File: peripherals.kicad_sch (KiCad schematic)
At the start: 6 parts, among them Q1 BSS138, SW2 SW_ACK, U7 TSOP384xx

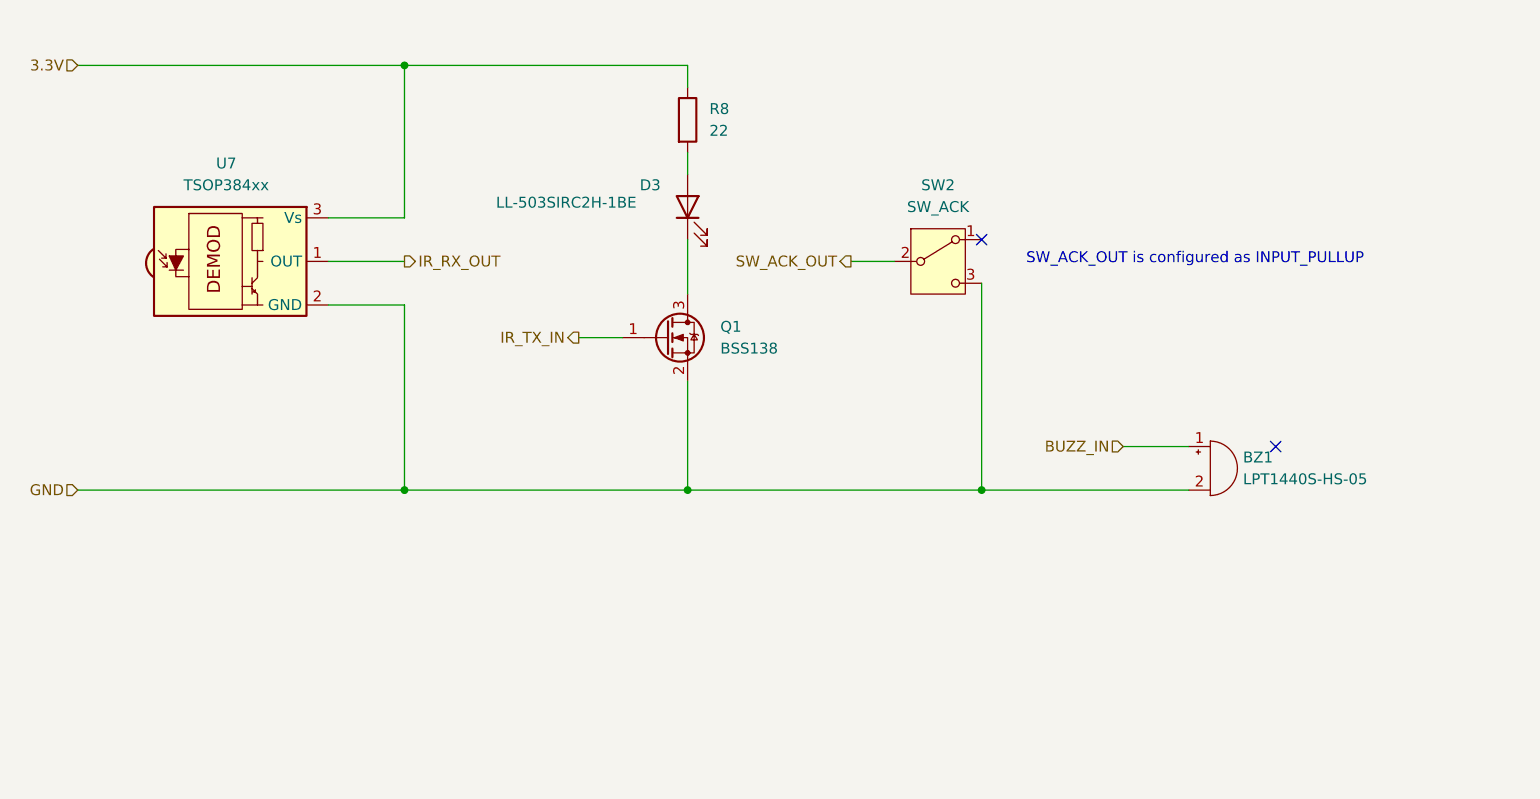
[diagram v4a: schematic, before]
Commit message: Cap and resistor for TSOP384x
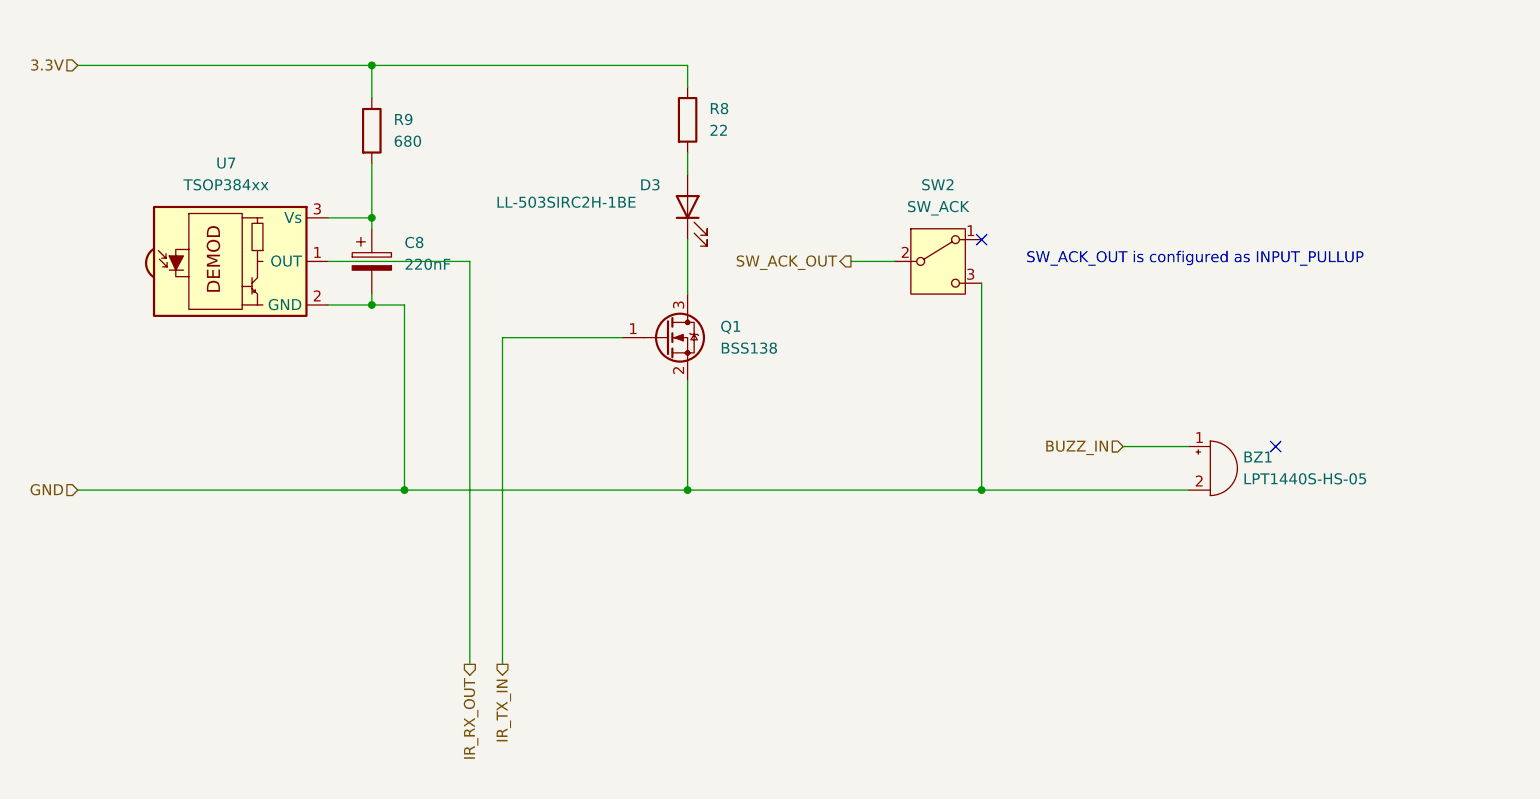
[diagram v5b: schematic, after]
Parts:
- added C8: 220nF, symbol Device:C_Polarized
- added R9: 680, symbol Device:R
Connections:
- net 3.3V: now also R9.1; no longer U7.3 (Vs)
- net GND: now also C8.2
- new net: C8.1, R9.2, U7.3 (Vs)
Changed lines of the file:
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@@
 	)
 	(junction
-		(at 81.28 38.1)
+		(at 77.47 38.1)
 		(diameter 0)
 		(color 0 0 0 0)
@@
 	)
 	(junction
+		(at 77.47 66.04)
+		(diameter 0)
+		(color 0 0 0 0)
+	)
+	(junction
 		(at 148.59 87.63)
 		(diameter 0)
@@
 		(color 0 0 0 0)
 	)
+	(junction
+		(at 77.47 55.88)
+		(diameter 0)
+		(color 0 0 0 0)
+	)
 	(no_connect
 		(at 148.59 58.42)
@@
 	(wire
 		(pts
-			(xy 101.6 69.85) (xy 106.68 69.85)
+			(xy 77.47 55.88) (xy 77.47 49.53)
 		)
 		(stroke
@@
 	(wire
 		(pts
+			(xy 77.47 64.77) (xy 77.47 66.04)
+		)
+		(stroke
+			(width 0)
+			(type default)
+		)
+	)
+	(wire
+		(pts
+			(xy 77.47 55.88) (xy 77.47 57.15)
+		)
+		(stroke
+			(width 0)
+			(type default)
+		)
+	)
+	(wire
+		(pts
 			(xy 114.3 74.93) (xy 114.3 87.63)
 		)
@@
 	(wire
 		(pts
+			(xy 92.71 69.85) (xy 92.71 107.95)
+		)
+		(stroke
+			(width 0)
+			(type default)
+		)
+	)
+	(wire
+		(pts
+			(xy 72.39 55.88) (xy 77.47 55.88)
+		)
+		(stroke
+			(width 0)
+			(type default)
+		)
+	)
+	(wire
+		(pts
+			(xy 77.47 66.04) (xy 81.28 66.04)
+		)
+		(stroke
+			(width 0)
+			(type default)
+		)
+	)
+	(wire
+		(pts
+			(xy 77.47 38.1) (xy 114.3 38.1)
+		)
+		(stroke
+			(width 0)
+			(type default)
+		)
+	)
+	(wire
+		(pts
+			(xy 88.9 60.96) (xy 88.9 107.95)
+		)
+		(stroke
+			(width 0)
+			(type default)
+		)
+	)
+	(wire
+		(pts
 			(xy 165.1 82.55) (xy 172.72 82.55)
 		)
@@
 	(wire
 		(pts
-			(xy 72.39 60.96) (xy 81.28 60.96)
-		)
-		(stroke
-			(width 0)
-			(type default)
-		)
-	)
-	(wire
-		(pts
-			(xy 81.28 38.1) (xy 114.3 38.1)
-		)
-		(stroke
-			(width 0)
-			(type default)
-		)
-	)
-	(wire
-		(pts
-			(xy 81.28 55.88) (xy 81.28 38.1)
+			(xy 92.71 69.85) (xy 106.68 69.85)
+		)
+		(stroke
+			(width 0)
+			(type default)
+		)
+	)
+	(wire
+		(pts
+			(xy 72.39 60.96) (xy 88.9 60.96)
+		)
+		(stroke
+			(width 0)
+			(type default)
+		)
+	)
+	(wire
+		(pts
+			(xy 43.18 38.1) (xy 77.47 38.1)
 		)
 		(stroke
@@
 	(wire
 		(pts
-			(xy 81.28 38.1) (xy 43.18 38.1)
+			(xy 77.47 38.1) (xy 77.47 41.91)
 		)
 		(stroke
@@
 	(wire
 		(pts
-			(xy 72.39 66.04) (xy 81.28 66.04)
-		)
-		(stroke
-			(width 0)
-			(type default)
-		)
-	)
-	(wire
-		(pts
-			(xy 72.39 55.88) (xy 81.28 55.88)
+			(xy 72.39 66.04) (xy 77.47 66.04)
 		)
 		(stroke
@@
 	(hierarchical_label "IR_RX_OUT"
 		(shape output)
-		(at 81.28 60.96 0)
+		(at 88.9 107.95 270)
 		(effects
 			(font
 				(size 1.27 1.27)
 			)
-			(justify left)
+			(justify right)
 		)
 	)
 	(hierarchical_label "IR_TX_IN"
 		(shape output)
-		(at 101.6 69.85 180)
+		(at 92.71 107.95 270)
 		(effects
 			(font
@@
 	)
 	(symbol
+		(lib_id "Device:R")
+		(at 77.47 45.72 0)
+		(unit 1)
+		(exclude_from_sim no)
+		(in_bom yes)
+		(on_board yes)
+		(dnp no)
+		(fields_autoplaced yes)
+		(property "Reference" "R9"
+			(at 80.01 44.4499 0)
+			(effects
+				(font
+					(size 1.27 1.27)
+				)
+				(justify left)
+			)
+		)
+		(property "Value" "680"
+			(at 80.01 46.9899 0)
+			(effects
+				(font
+					(size 1.27 1.27)
+				)
+				(justify left)
+			)
+		)
+		(property "Footprint" ""
+			(at 75.692 45.72 90)
+			(effects
+				(font
+					(size 1.27 1.27)
+				)
+				(hide yes)
+			)
+		)
+		(property "Datasheet" "~"
+			(at 77.47 45.72 0)
+			(effects
+				(font
+					(size 1.27 1.27)
+				)
+				(hide yes)
+			)
+		)
+		(property "Description" "Resistor"
+			(at 77.47 45.72 0)
+			(effects
+				(font
+					(size 1.27 1.27)
+				)
+				(hide yes)
+			)
+		)
+		(pin "1"
+		)
+		(pin "2"
+		)
+		(instances
+			(project ""
+				(path "/64404f27-cfd6-41d9-8edb-810ebab8cc14/ed770b04-6f81-410b-b0ec-7aa50308ff69"
+					(reference "R9")
+					(unit 1)
+				)
+			)
+		)
+	)
+	(symbol
 		(lib_id "Interface_Optical:TSOP384xx")
 		(at 62.23 60.96 0)
@@
 					(unit 1)
 				)
+			)
+		)
+	)
+	(symbol
+		(lib_id "Device:C_Polarized")
+		(at 77.47 60.96 0)
+		(unit 1)
+		(exclude_from_sim no)
+		(in_bom yes)
+		(on_board yes)
+		(dnp no)
+		(fields_autoplaced yes)
+		(property "Reference" "C8"
+			(at 81.28 58.8009 0)
+			(effects
+				(font
+					(size 1.27 1.27)
+				)
+				(justify left)
+			)
+		)
+		(property "Value" "220nF"
+			(at 81.28 61.3409 0)
+			(effects
+				(font
+					(size 1.27 1.27)
+				)
+				(justify left)
+			)
+		)
+		(property "Footprint" ""
+			(at 78.4352 64.77 0)
+			(effects
+				(font
+					(size 1.27 1.27)
+				)
+				(hide yes)
+			)
+		)
+		(property "Datasheet" "~"
+			(at 77.47 60.96 0)
+			(effects
+				(font
+					(size 1.27 1.27)
+				)
+				(hide yes)
+			)
+		)
+		(property "Description" "Polarized capacitor"
+			(at 77.47 60.96 0)
+			(effects
+				(font
+					(size 1.27 1.27)
+				)
+				(hide yes)
+			)
+		)
+		(pin "1"
+		)
+		(pin "2"
+		)
+		(instances
+			(project ""
+				(path "/64404f27-cfd6-41d9-8edb-810ebab8cc14/ed770b04-6f81-410b-b0ec-7aa50308ff69"
+					(reference "C8")
+					(unit 1)
+				)

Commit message: Moved some components around for better readability.
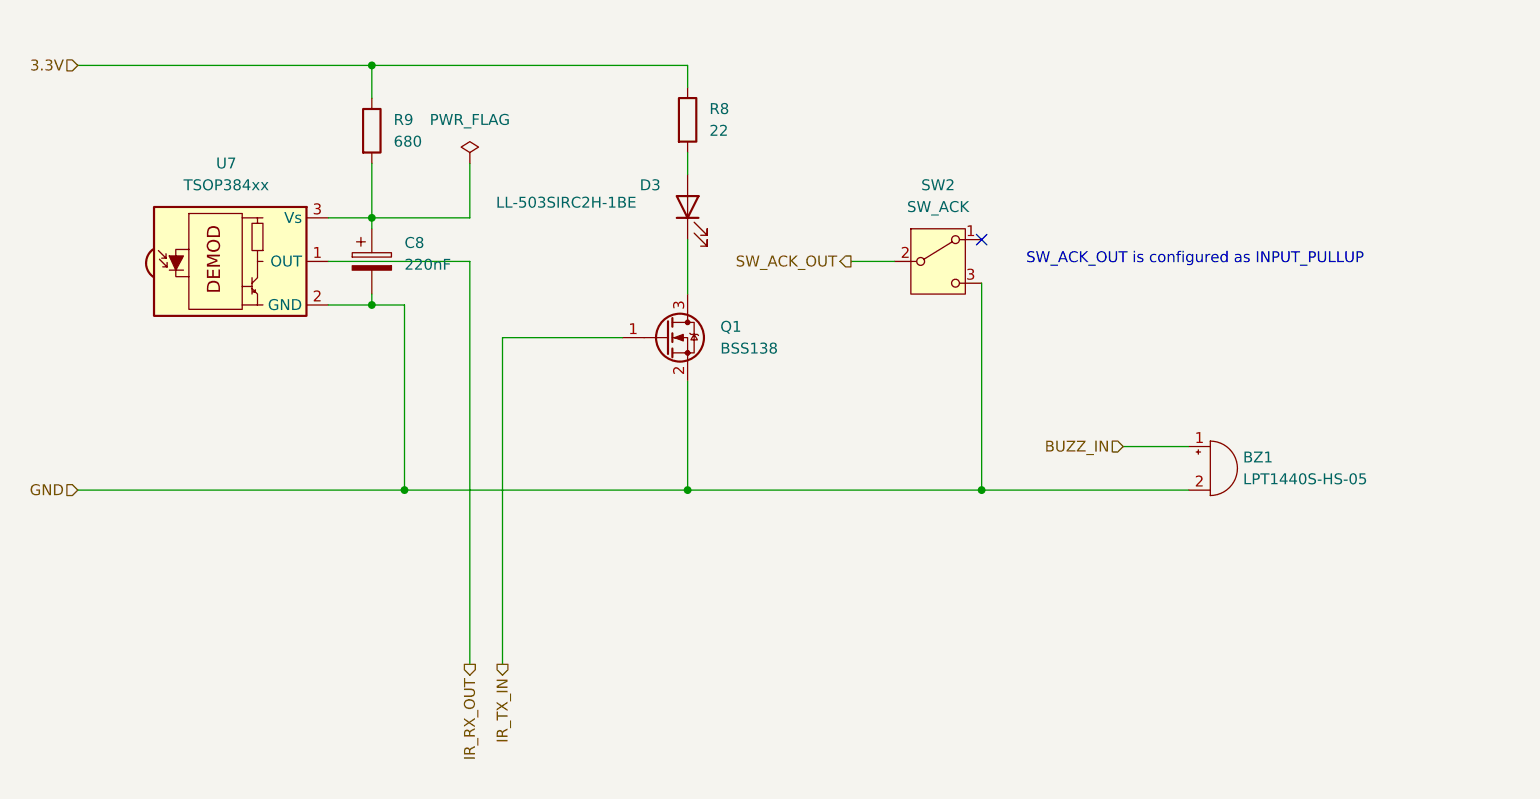
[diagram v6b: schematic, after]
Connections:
- no-connect marks 2 -> 1
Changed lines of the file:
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@@
 		(at 148.59 58.42)
 	)
-	(no_connect
-		(at 182.88 82.55)
-	)
 	(wire
 		(pts
@@
 	(wire
 		(pts
+			(xy 88.9 49.53) (xy 88.9 55.88)
+		)
+		(stroke
+			(width 0)
+			(type default)
+		)
+	)
+	(wire
+		(pts
 			(xy 77.47 55.88) (xy 77.47 57.15)
 		)
@@
 		(pts
 			(xy 72.39 66.04) (xy 77.47 66.04)
+		)
+		(stroke
+			(width 0)
+			(type default)
+		)
+	)
+	(wire
+		(pts
+			(xy 88.9 55.88) (xy 77.47 55.88)
 		)
 		(stroke
@@
 					(unit 1)
 				)
+			)
+		)
+	)
+	(symbol
+		(lib_id "power:PWR_FLAG")
+		(at 88.9 49.53 0)
+		(unit 1)
+		(exclude_from_sim no)
+		(in_bom yes)
+		(on_board yes)
+		(dnp no)
+		(fields_autoplaced yes)
+		(property "Reference" "#FLG03"
+			(at 88.9 47.625 0)
+			(effects
+				(font
+					(size 1.27 1.27)
+				)
+				(hide yes)
+			)
+		)
+		(property "Value" "PWR_FLAG"
+			(at 88.9 44.45 0)
+			(effects
+				(font
+					(size 1.27 1.27)
+				)
+			)
+		)
+		(property "Footprint" ""
+			(at 88.9 49.53 0)
+			(effects
+				(font
+					(size 1.27 1.27)
+				)
+				(hide yes)
+			)
+		)
+		(property "Datasheet" "~"
+			(at 88.9 49.53 0)
+			(effects
+				(font
+					(size 1.27 1.27)
+				)
+				(hide yes)
+			)
+		)
+		(property "Description" "Special symbol for telling ERC where power comes from"
+			(at 88.9 49.53 0)
+			(effects
+				(font
+					(size 1.27 1.27)
+				)
+				(hide yes)
+			)
+		)
+		(pin "1"
+		)
+		(instances
+			(project ""
+				(path "/64404f27-cfd6-41d9-8edb-810ebab8cc14/ed770b04-6f81-410b-b0ec-7aa50308ff69"
+					(reference "#FLG03")
+					(unit 1)
+				)

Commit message: Updated README.
Reworked the circuit around CH224K per datasheet an example schematics.
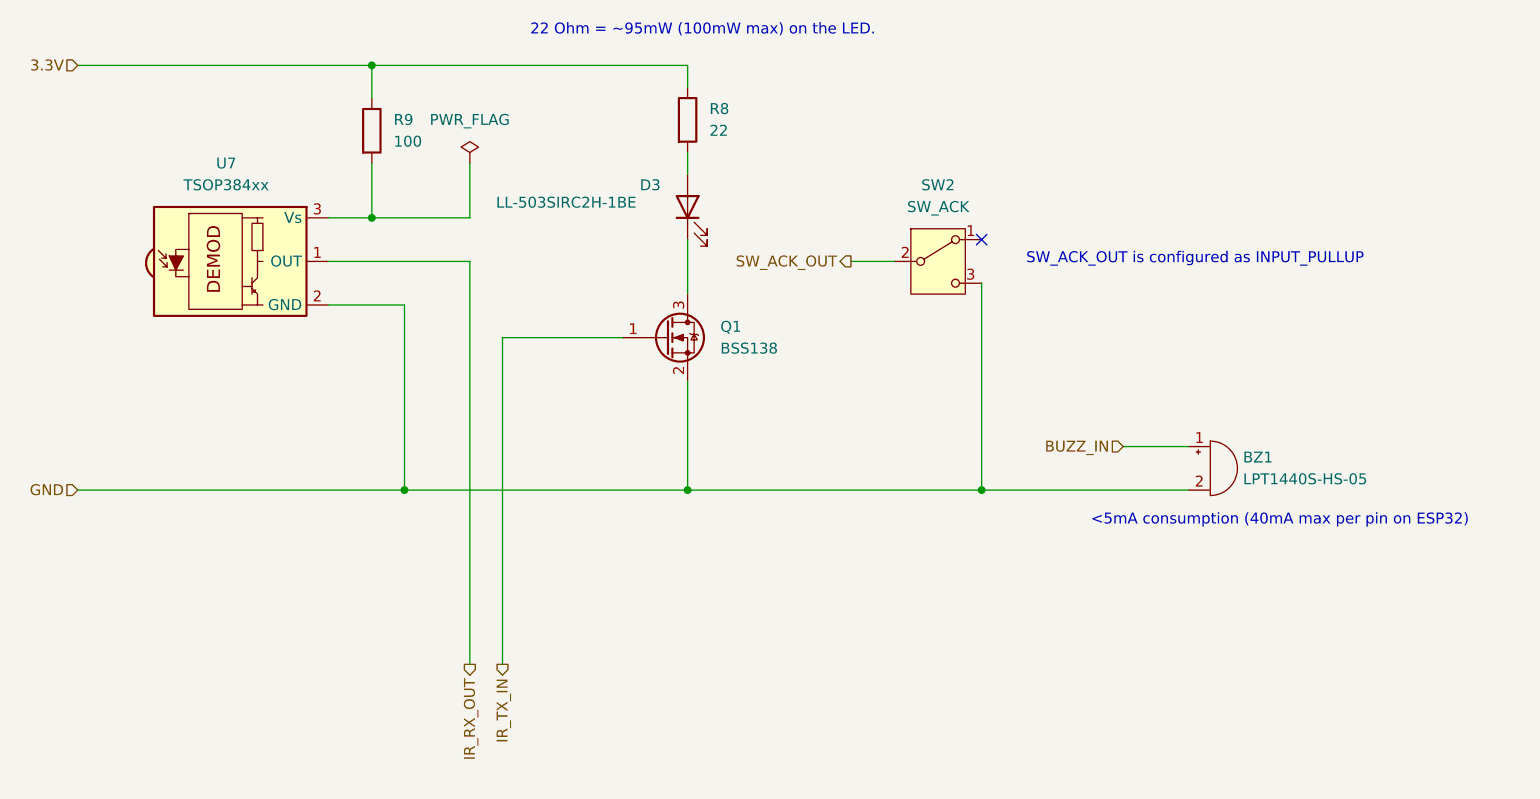
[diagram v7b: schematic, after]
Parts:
- removed C8: 220nF, symbol Device:C_Polarized
- R9: value 680 -> 100
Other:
- note added: "22 Ohm = ~95mW (100mW max) on the LED."
- note added: "<5mA consumption (40mA max per pin on ESP32)"
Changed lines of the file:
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@@
+		)
+	)
+	(text "22 Ohm = ~95mW (100mW max) on the LED."
+		(exclude_from_sim no)
+		(at 116.078 34.036 0)
+		(effects
+			(font
+				(size 1.27 1.27)
+			)
+		)
+	)
+	(text "<5mA consumption (40mA max per pin on ESP32)\n"
+		(exclude_from_sim no)
+		(at 183.388 91.186 0)
+		(effects
+			(font
+				(size 1.27 1.27)
+			)
 		)
 	)
@@
 	)
 	(junction
-		(at 77.47 66.04)
-		(diameter 0)
-		(color 0 0 0 0)
-	)
-	(junction
 		(at 148.59 87.63)
 		(diameter 0)
@@
 	(wire
 		(pts
-			(xy 77.47 64.77) (xy 77.47 66.04)
-		)
-		(stroke
-			(width 0)
-			(type default)
-		)
-	)
-	(wire
-		(pts
 			(xy 88.9 49.53) (xy 88.9 55.88)
 		)
@@
 	(wire
 		(pts
-			(xy 77.47 55.88) (xy 77.47 57.15)
-		)
-		(stroke
-			(width 0)
-			(type default)
-		)
-	)
-	(wire
-		(pts
 			(xy 114.3 74.93) (xy 114.3 87.63)
 		)
@@
 	(wire
 		(pts
-			(xy 77.47 66.04) (xy 81.28 66.04)
+			(xy 72.39 66.04) (xy 81.28 66.04)
 		)
 		(stroke
@@
 		(pts
 			(xy 81.28 87.63) (xy 43.18 87.63)
-		)
-		(stroke
-			(width 0)
-			(type default)
-		)
-	)
-	(wire
-		(pts
-			(xy 72.39 66.04) (xy 77.47 66.04)
 		)
 		(stroke
@@
 			)
 		)
-		(property "Value" "680"
+		(property "Value" "100"
 			(at 80.01 46.9899 0)
 			(effects
@@
 					(unit 1)
 				)
-			)
-		)
-	)
-	(symbol
-		(lib_id "Device:C_Polarized")
-		(at 77.47 60.96 0)
-		(unit 1)
-		(exclude_from_sim no)
-		(in_bom yes)
-		(on_board yes)
-		(dnp no)
-		(fields_autoplaced yes)
-		(property "Reference" "C8"
-			(at 81.28 58.8009 0)
-			(effects
-				(font
-					(size 1.27 1.27)
-				)
-				(justify left)
-			)
-		)
-		(property "Value" "220nF"
-			(at 81.28 61.3409 0)
-			(effects
-				(font
-					(size 1.27 1.27)
-				)
-				(justify left)
-			)
-		)
-		(property "Footprint" ""
-			(at 78.4352 64.77 0)
-			(effects
-				(font
-					(size 1.27 1.27)
-				)
-				(hide yes)
-			)
-		)
-		(property "Datasheet" "~"
-			(at 77.47 60.96 0)
-			(effects
-				(font
-					(size 1.27 1.27)
-				)
-				(hide yes)
-			)
-		)
-		(property "Description" "Polarized capacitor"
-			(at 77.47 60.96 0)
-			(effects
-				(font
-					(size 1.27 1.27)
-				)
-				(hide yes)
-			)
-		)
-		(pin "1"
-		)
-		(pin "2"
-		)
-		(instances
-			(project ""
-				(path "/64404f27-cfd6-41d9-8edb-810ebab8cc14/ed770b04-6f81-410b-b0ec-7aa50308ff69"
-					(reference "C8")
-					(unit 1)
-				)

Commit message: Reorganized board to be on one sheet.
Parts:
- removed BZ1: LPT1440S-HS-05, symbol Device:Buzzer
- removed D3: LL-503SIRC2H-1BE, symbol Device:LED
- removed Q1: BSS138, Package_TO_SOT_SMD:SOT-23, symbol Transistor_FET:BSS138
- removed R8: 22, symbol Device:R
- removed R9: 100, symbol Device:R
- removed SW2: SW_ACK, symbol Switch:SW_SPDT
- removed U7: TSOP384xx, OptoDevice:Vishay_MINICAST-3Pin, symbol Interface_Optical:TSOP384xx
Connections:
- no-connect marks 1 -> 0
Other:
- note removed: "22 Ohm = ~95mW (100mW max) on the LED."
- note removed: "<5mA consumption (40mA max per pin on ESP32)"
- note removed: "SW_ACK_OUT is configured as INPUT_PULLUP"
